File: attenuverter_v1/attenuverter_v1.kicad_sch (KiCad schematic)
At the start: 16 parts, among them J1 Conn_02x05_Odd_Even, J2 AudioJack2_SwitchT, J3 AudioJack2_SwitchT, J4 AudioJack2_SwitchT, J5 AudioJack2_SwitchT, J6 AudioJack2_SwitchT, J7 AudioJack2_SwitchT

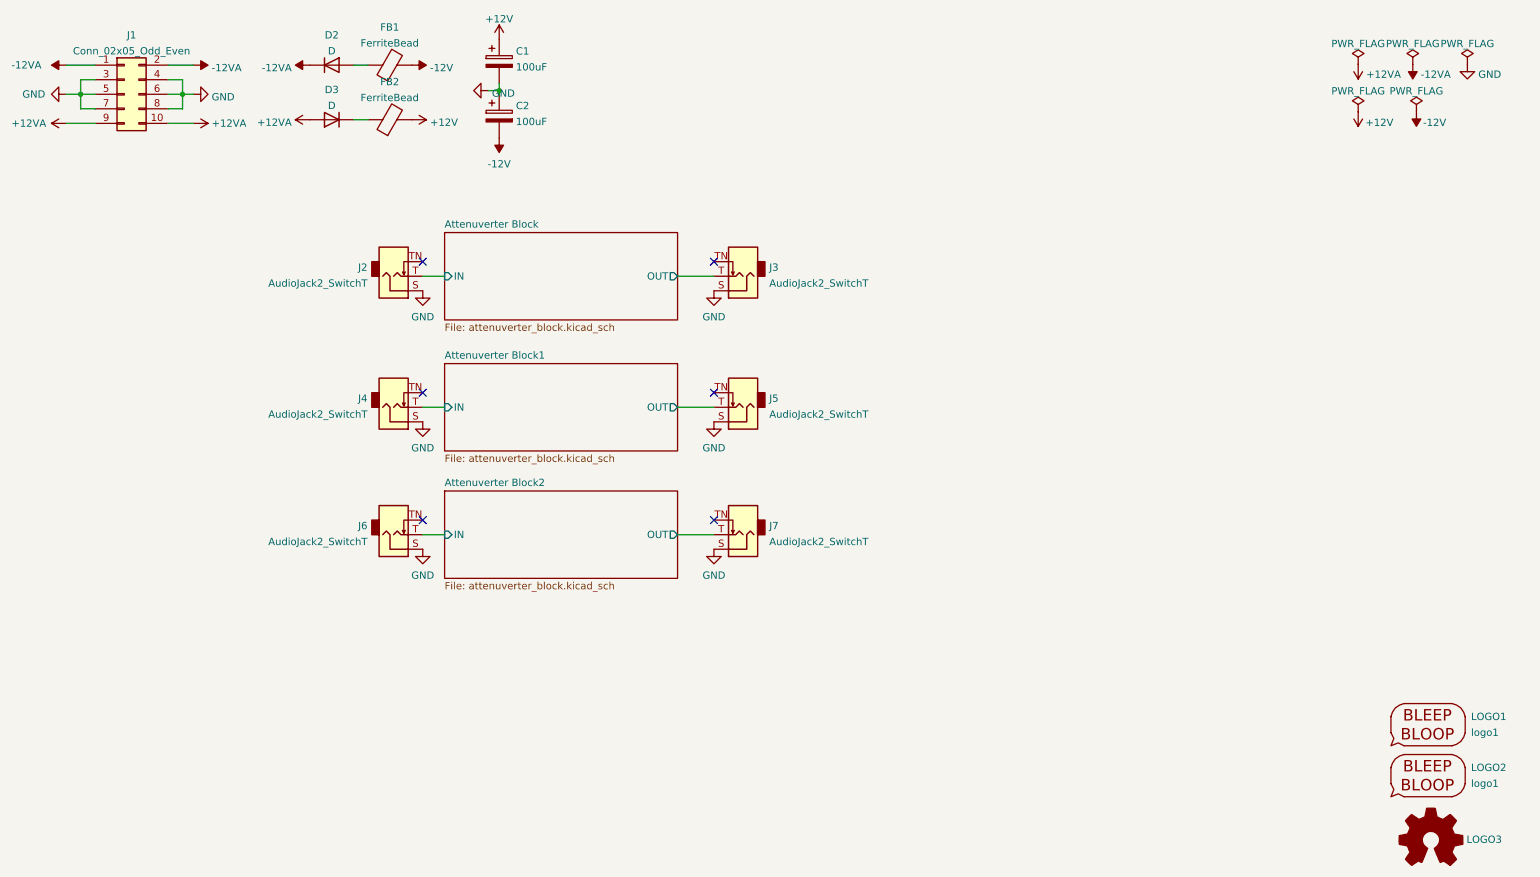
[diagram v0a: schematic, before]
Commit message: Silkscreen cleanup and labeling
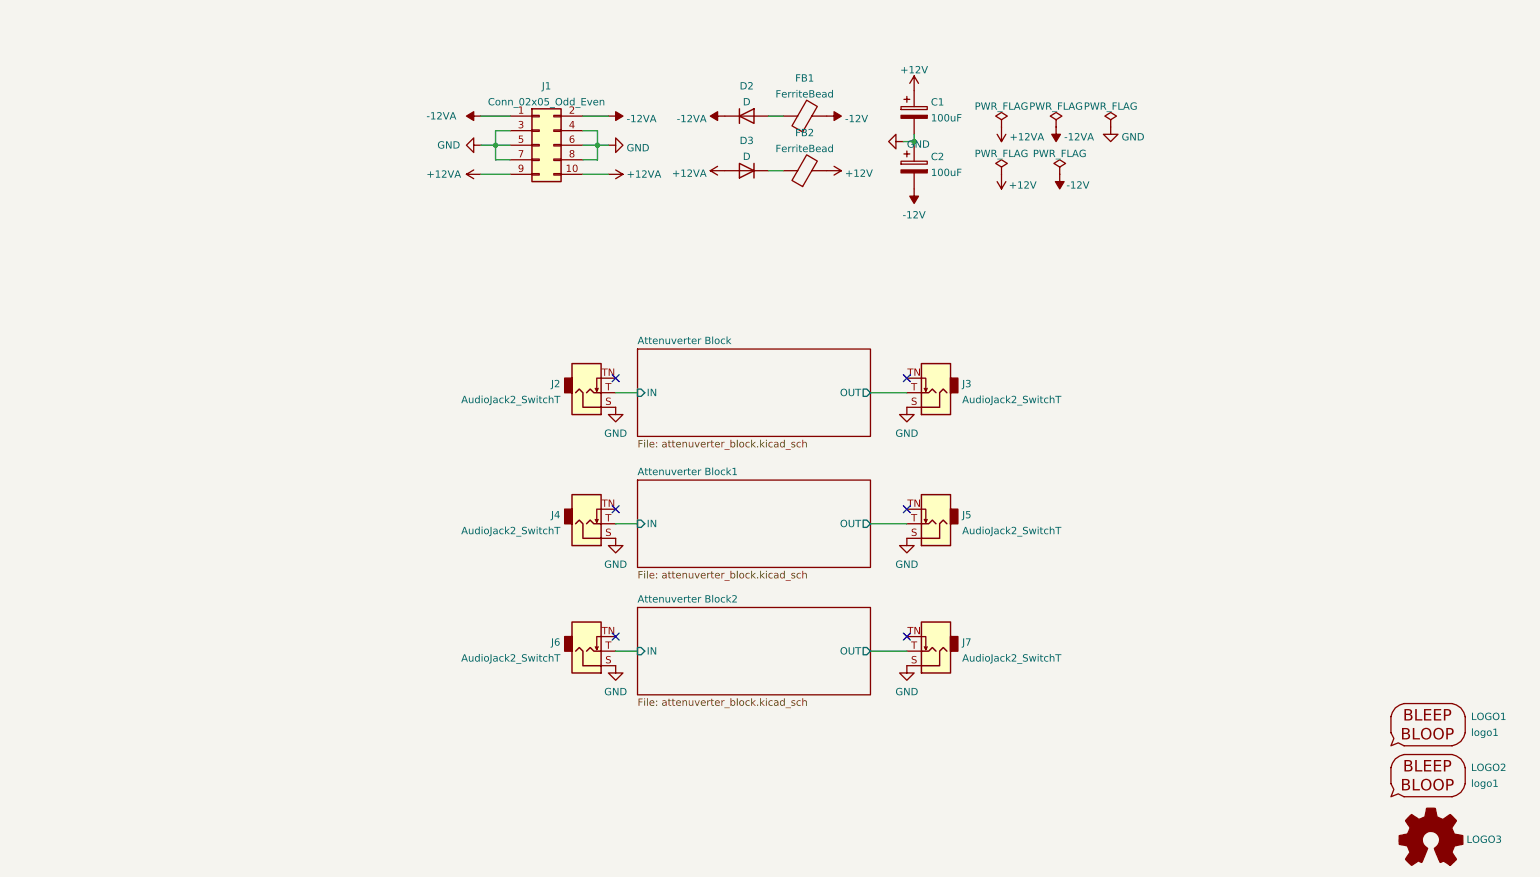
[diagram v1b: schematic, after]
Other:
- title: Annetuverter -> Triple Annetuverter
- moved on the sheet: C1, C2, D2, D3, FB1, FB2, J1, J2, J3, J4, J5, J6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

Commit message: Geographic rename
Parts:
- renumbered C1 to C4, C2 to C5, D2 to D1, D3 to D2, J1 to J8, LOGO3 to LOGO100, LOGO2 to LOGO101, LOGO1 to LOGO102
